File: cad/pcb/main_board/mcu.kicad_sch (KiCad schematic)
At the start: 2 parts, among them U1 STM32F401R_B-C_Tx

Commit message: VDDA, BOOT SEL
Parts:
- added C12, C13: C, symbol Device:C
- added C9: 0u1F, symbol Device:C
- added R1, R2: 10kR, symbol Device:R
- added SW1: SW_DIP_x02, symbol Switch:SW_DIP_x02
- added SWRST1: SW_Push, symbol Switch:SW_Push
- added Y1: Crystal_GND23, symbol Device:Crystal_GND23
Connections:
- net VDD: now also SW1.1, SW1.2
- net VSS: now also C12.2, C13.2, C9.1, SWRST1.2, Y1.2, Y1.3
- net BOOT1: now reaches U1.28 (PB2)
- net BOOT1: now also R2.2
- net USB_D-: now reaches U1.44 (PA11)
- net USB_D+: now reaches U1.45 (PA12)
- net at U1.5 (PH0): now also C12.1, Y1.1
- net at U1.6 (PH1): now also C13.1, Y1.4
- net BOOT0: now reaches U1.60 (BOOT0)
- net BOOT0: now also R1.2
- net at U1.7 (NRST): now also C9.2, SWRST1.1
- net ADC1_IN0 renamed ADC_IN0
- net ADC1_IN1 renamed ADC_IN1
- net ADC1_IN10 renamed ADC_IN10
- net ADC1_IN11 renamed ADC_IN11
- net ADC1_IN12 renamed ADC_IN12
- net ADC1_IN13 renamed ADC_IN13
- net ADC1_IN14 renamed ADC_IN14
- net ADC1_IN15 renamed ADC_IN15
- net ADC1_IN2 renamed ADC_IN2
- net ADC1_IN3 renamed ADC_IN3
- net ADC1_IN4 renamed ADC_IN4
- net ADC1_IN5 renamed ADC_IN5
- net ADC1_IN6 renamed ADC_IN6
- net ADC1_IN7 renamed ADC_IN7
- net ADC1_IN8 renamed ADC_IN8
- net ADC1_IN9 renamed ADC_IN9
- new net: R2.1, SW1.3
- new net: R1.1, SW1.4
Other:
- sheet PowerSupply ports: added VDDA; removed VBAT

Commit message: HSE, usb, TC
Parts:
- C12: value C -> CL1
- C13: value C -> CL2
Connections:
- net USB_ID: now reaches U1.43 (PA10)
- no-connect marks 0 -> 25
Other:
- note added: "C_L = CL1 * CL2 / (CL1 + CL2) + C_S C_L Load Capacitance C_S Parasitics"
- note added: "ESR < 1R"
- note added: "RM0368 details Clock Registers + Clock Tree HSE needed for USB HSE/PLLM * PLLN/PLLQ = 48 MHz 192 <= PLLN <= 432 2 <= PLLQ <= 15 2 <= PLLM <= 63 24 MHz / 8 (PLLM = 8) = 3 MHz 3 MHz * (8 * 8 (PLLN = 256)) = 24 MHz * 8 24 Mhz * 8 / 4 (PLLQ) = 48 MHz"
- moved on the sheet: C1, C12, C13, C9, SWRST1, U1, Y1

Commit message: Thermo Couple Pins
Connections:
- net VBAT is gone; now on net VDD: U1.1 (VBAT)
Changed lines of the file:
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@@
+    )
+  )
+  (global_label "VDD" (shape input) (at 164.465 52.07 90) (fields_autoplaced)
+    (effects (font (size 1.27 1.27)) (justify left))
+    (property "Intersheetrefs" "${INTERSHEET_REFS}" (at 164.465 45.4562 90)
+      (effects (font (size 1.27 1.27)) (justify left) hide)
     )
   )
@@
       (effects (font (size 1.27 1.27)) (justify left) hide)
     )
-  )
-  (global_label "VBAT" (shape input) (at 164.465 52.07 90) (fields_autoplaced)
-    (effects (font (size 1.27 1.27)) (justify left))
-    (property "Intersheetrefs" "${INTERSHEET_REFS}" (at 164.465 44.67 90)
-      (effects (font (size 1.27 1.27)) (justify left) hide)
-    )

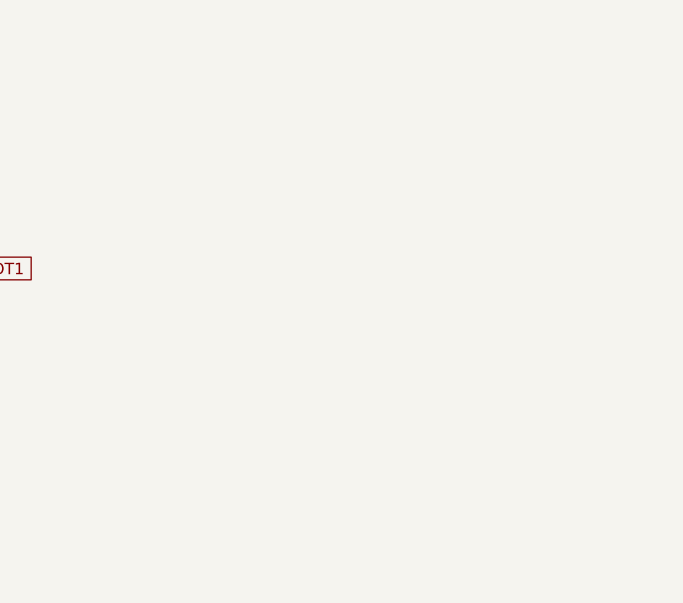
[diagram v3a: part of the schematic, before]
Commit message: Adding Voltage Regulators, Adding SD Card Symbol
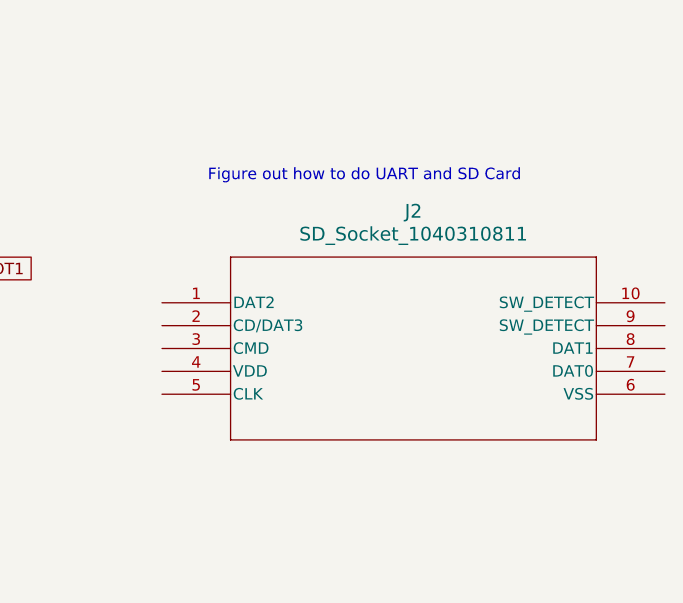
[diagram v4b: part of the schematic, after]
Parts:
- added J2: SD_Socket_1040310811, 104031-0811_MOL, symbol local:SD_Socket_1040310811
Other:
- note added: "Figure out how to do UART and SD Card"
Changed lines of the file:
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@@
+    (effects (font (size 1.27 1.27)) (justify left bottom))
+  )
+  (text "Figure out how to do UART and SD Card\n" (at 225.425 98.425 0)
     (effects (font (size 1.27 1.27)) (justify left bottom))
   )
@@
         )
       )
+    )
+  )
+  (symbol (lib_id "local:SD_Socket_1040310811") (at 220.345 111.76 0) (unit 1)
+    (in_bom yes) (on_board yes) (dnp no) (fields_autoplaced)
+    (property "Reference" "J2" (at 248.285 101.6 0)
+      (effects (font (size 1.524 1.524)))
+    )
+    (property "Value" "SD_Socket_1040310811" (at 248.285 104.14 0)
+      (effects (font (size 1.524 1.524)))
+    )
+    (property "Footprint" "104031-0811_MOL" (at 220.345 111.76 0)
+      (effects (font (size 1.27 1.27) italic) hide)
+    )
+    (property "Datasheet" "1040310811" (at 220.345 111.76 0)
+      (effects (font (size 1.27 1.27) italic) hide)
+    )
+    (pin "1")
+    (pin "10")
+    (pin "2")
+    (pin "3")
+    (pin "4")
+    (pin "5")
+    (pin "6")
+    (pin "7")
+    (pin "8")
+    (pin "9")
+    (instances
+      (project "main_board"
+        (path "/6c1b8035-64fa-4797-a506-5c9583cb241c/89e1b759-e3da-4961-90e8-6f92bf79e795"
+          (reference "J2") (unit 1)
+        )
+      )

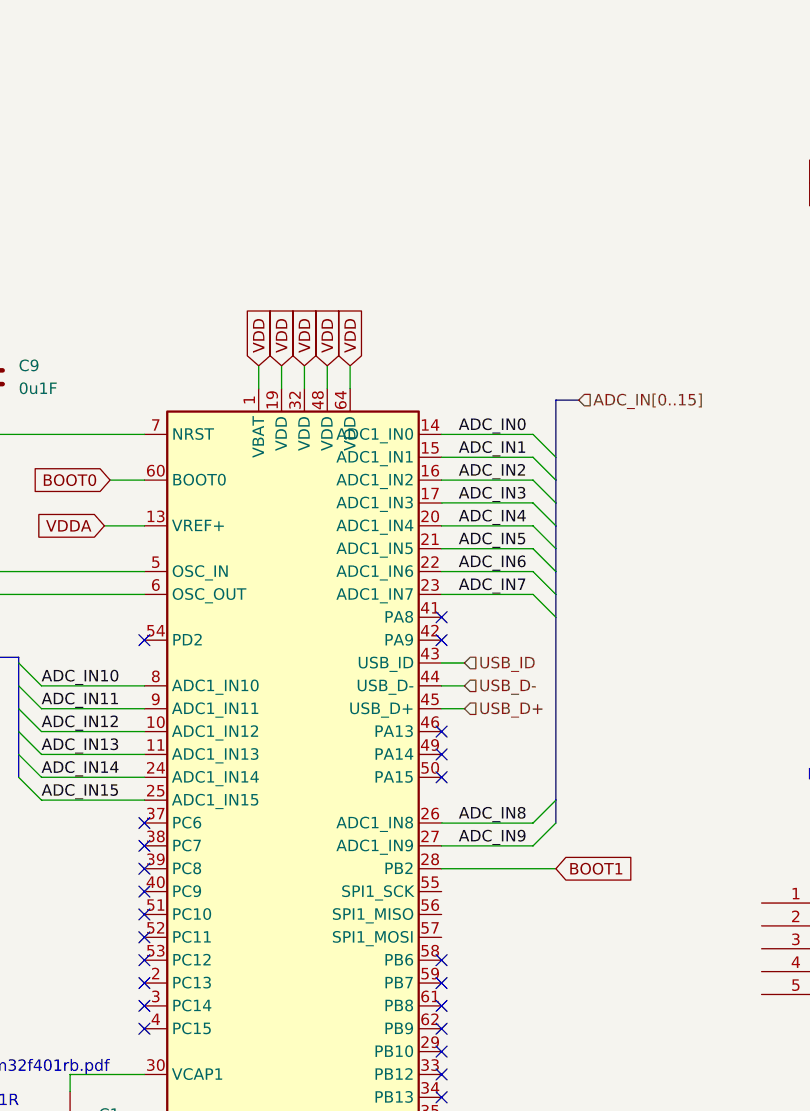
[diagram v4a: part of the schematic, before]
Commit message: Add usb an/ add missing connections note
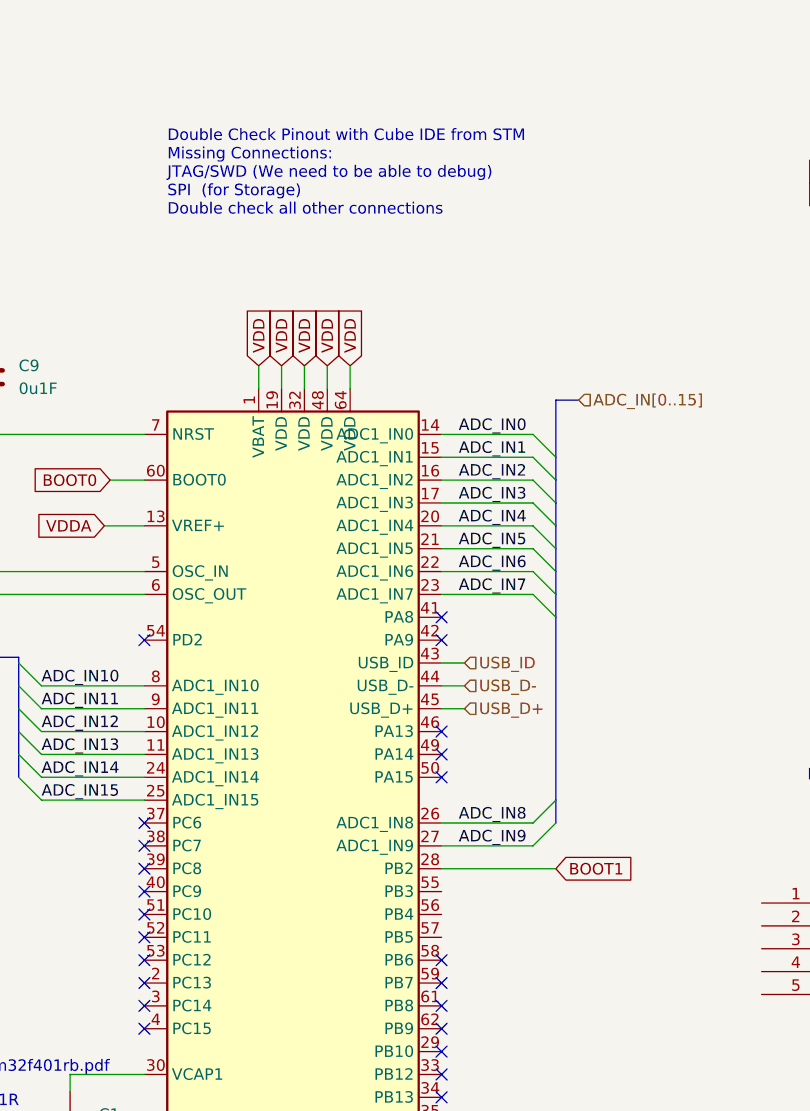
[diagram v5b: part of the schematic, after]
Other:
- note added: "Double Check Pinout with Cube IDE from STM Missing Connections: JTAG/SWD (We need to be able to debug) SPI (for Storage) Double check all other connections"
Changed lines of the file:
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@@
+    (effects (font (size 1.27 1.27)) (justify left bottom))
+  )
+  (text "Double Check Pinout with Cube IDE from STM\nMissing Connections:\nJTAG/SWD (We need to be able to debug)\nSPI  (for Storage)\nDouble check all other connections"
+    (at 154.305 35.56 0)
     (effects (font (size 1.27 1.27)) (justify left bottom))
   )
@@
     (pin "53")
     (pin "54")
-    (pin "55" (alternate "SPI1_SCK"))
-    (pin "56" (alternate "SPI1_MISO"))
-    (pin "57" (alternate "SPI1_MOSI"))
+    (pin "55")
+    (pin "56")
+    (pin "57")
     (pin "58")
     (pin "59")

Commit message: Add Aisler files
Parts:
- removed J2: SD_Socket_1040310811, 104031-0811_MOL, symbol local:SD_Socket_1040310811
- C1, C12, C13, C9: footprint (none) -> Capacitor_SMD:C_0805_2012Metric
- R1, R2: footprint (none) -> Resistor_SMD:R_0805_2012Metric
- SW1: footprint (none) -> Button_Switch_SMD:SW_DIP_SPSTx02_Slide_6.7x6.64mm_W6.73mm_P2.54mm_LowProfile_JPin
- SWRST1: footprint (none) -> Button_Switch_THT:SW_PUSH_6mm
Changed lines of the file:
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@@
     (effects (font (size 1.27 1.27)) (justify left bottom))
   )
-  (text "Figure out how to do UART and SD Card\n" (at 225.425 98.425 0)
+  (text "Figure out how to do UART and SD Card\n" (at 154.305 24.765 0)
     (effects (font (size 1.27 1.27)) (justify left bottom))
   )
@@
       (effects (font (size 1.27 1.27)))
     )
-    (property "Footprint" "" (at 257.81 31.242 90)
+    (property "Footprint" "Resistor_SMD:R_0805_2012Metric" (at 257.81 31.242 90)
       (effects (font (size 1.27 1.27)) hide)
     )
@@
       (effects (font (size 1.27 1.27)))
     )
-    (property "Footprint" "" (at 257.81 32.258 90)
+    (property "Footprint" "Resistor_SMD:R_0805_2012Metric" (at 257.81 32.258 90)
       (effects (font (size 1.27 1.27)) hide)
     )
@@
       (effects (font (size 1.27 1.27)) (justify left))
     )
-    (property "Footprint" "" (at 134.9502 57.15 0)
+    (property "Footprint" "Capacitor_SMD:C_0805_2012Metric" (at 134.9502 57.15 0)
       (effects (font (size 1.27 1.27)) hide)
     )
@@
       (effects (font (size 1.27 1.27)) (justify right))
     )
-    (property "Footprint" "" (at 109.22 52.07 0)
+    (property "Footprint" "Button_Switch_THT:SW_PUSH_6mm" (at 109.22 52.07 0)
       (effects (font (size 1.27 1.27)) hide)
     )
@@
     )
   )
-  (symbol (lib_id "local:SD_Socket_1040310811") (at 220.345 111.76 0) (unit 1)
-    (in_bom yes) (on_board yes) (dnp no) (fields_autoplaced)
-    (property "Reference" "J2" (at 248.285 101.6 0)
-      (effects (font (size 1.524 1.524)))
-    )
-    (property "Value" "SD_Socket_1040310811" (at 248.285 104.14 0)
-      (effects (font (size 1.524 1.524)))
-    )
-    (property "Footprint" "104031-0811_MOL" (at 220.345 111.76 0)
-      (effects (font (size 1.27 1.27) italic) hide)
-    )
-    (property "Datasheet" "1040310811" (at 220.345 111.76 0)
-      (effects (font (size 1.27 1.27) italic) hide)
-    )
-    (pin "1")
-    (pin "10")
-    (pin "2")
-    (pin "3")
-    (pin "4")
-    (pin "5")
-    (pin "6")
-    (pin "7")
-    (pin "8")
-    (pin "9")
-    (instances
-      (project "main_board"
-        (path "/6c1b8035-64fa-4797-a506-5c9583cb241c/89e1b759-e3da-4961-90e8-6f92bf79e795"
-          (reference "J2") (unit 1)
-        )
-      )
-    )
-  )
   (symbol (lib_id "Device:C") (at 111.125 79.375 0) (unit 1)
     (in_bom yes) (on_board yes) (dnp no) (fields_autoplaced)
@@
       (effects (font (size 1.27 1.27)) (justify left))
     )
-    (property "Footprint" "" (at 112.0902 83.185 0)
+    (property "Footprint" "Capacitor_SMD:C_0805_2012Metric" (at 112.0902 83.185 0)
       (effects (font (size 1.27 1.27)) hide)
     )
@@
       (effects (font (size 1.27 1.27)) (justify left))
     )
-    (property "Footprint" "" (at 94.3102 83.185 0)
+    (property "Footprint" "Capacitor_SMD:C_0805_2012Metric" (at 94.3102 83.185 0)
       (effects (font (size 1.27 1.27)) hide)
     )
@@
       (effects (font (size 1.27 1.27)) (justify left))
     )
-    (property "Footprint" "" (at 144.4752 140.335 0)
+    (property "Footprint" "Capacitor_SMD:C_0805_2012Metric" (at 144.4752 140.335 0)
       (effects (font (size 1.27 1.27)) hide)
     )
@@
       (effects (font (size 1.27 1.27)))
     )
-    (property "Footprint" "" (at 244.475 33.02 0)
-      (effects (font (size 1.27 1.27)) hide)
-    )
+    (property "Footprint" "Button_Switch_SMD:SW_DIP_SPSTx02_Slide_6.7x6.64mm_W6.73mm_P2.54mm_LowProfile_JPin" (at 244.475 33.02 0)
+      (effects (font (size 1.27 1.27)) hide)
+    )
